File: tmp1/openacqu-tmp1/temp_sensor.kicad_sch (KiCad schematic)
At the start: 2 parts, among them J3 SJ-3524-SMT, U7 MCP9600T-E_MX

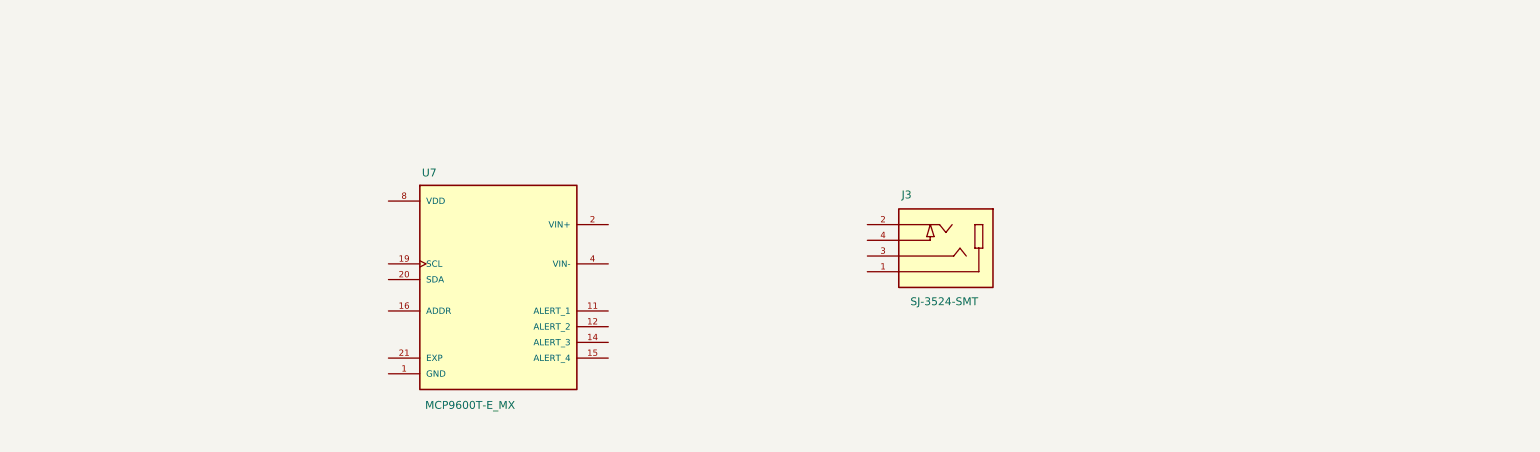
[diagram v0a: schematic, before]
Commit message: Completed layout for the TMP1
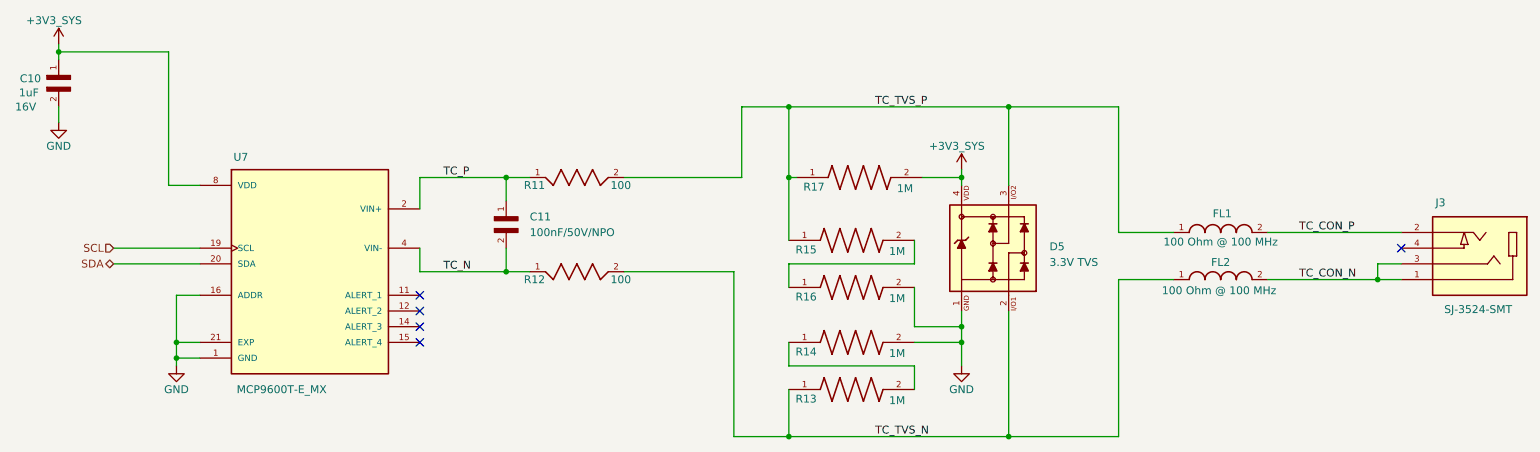
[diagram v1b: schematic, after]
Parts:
- added C10: 1uF, openacqu_footprints:CAPC1005X55N, symbol CL05A105KO5NNNC:CL05A105KO5NNNC
- added C11: 100nF/50V/NPO, CAPC3216X95N, symbol GRM3195C1H104JA05D:GRM3195C1H104JA05D
- added D5: 3.3V TVS, WE-TVS_SOT143-4L, symbol WE-TVS-HS_SOT143-4L_8240136:WE-TVS-HS_SOT143-4L_8240136
- added FL1, FL2: 100 Ohm @ 100 MHz, BEADC1608X65N, symbol BLM18EG101TN1D:BLM18EG101TN1D
- added R11, R12: 100, RESC1005X40, symbol RC0402FR-07100RL:RC0402FR-07100RL
- added R13, R14, R15, R16, R17: 1M, RESC1005X40N, symbol RC0402FR-071ML:RC0402FR-071ML
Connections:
- net GND is gone; now on net EXP: U7.1 (GND), U7.10 (GND), U7.13 (GND), U7.17 (GND), U7.18 (GND), U7.3 (GND), U7.5 (GND), U7.6 (GND), U7.7 (GND), U7.9 (GND)
- net EXP: now also U7.16 (ADDR), C10.2, D5.1, R14.2, R16.2
- net SCL: now reaches U7.19 (SCL)
- net TC_P: now reaches U7.2 (VIN+)
- net TC_P: now also C11.1, R11.1
- net SDA: now reaches U7.20 (SDA)
- net TC_N: now reaches U7.4 (VIN-)
- net TC_N: now also C11.2, R12.1
- net +3V3_SYS: now reaches U7.8 (VDD)
- net +3V3_SYS: now also C10.1, D5.4, R17.2
- net TC_CON_N: now reaches J3.1
- net TC_CON_N: now also J3.3, FL2.2
- net TC_CON_P: now reaches J3.2
- net TC_CON_P: now also FL1.2
- new net: R13.2, R14.1
- new net: R15.2, R16.1
- new net TC_TVS_N: D5.2, FL2.1, R12.2, R13.1
- new net TC_TVS_P: D5.3, FL1.1, R11.2, R15.1, R17.1
- no-connect marks 0 -> 5
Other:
- moved on the sheet: J3, U7

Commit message: Updated symbols with JLCPCB part numbers
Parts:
- C10: JLCPN (none) -> C29266
- C11: JLCPN (none) -> C363929
- D5: JLCPN (none) -> C1975797
- FL1, FL2: JLCPN (none) -> C76893
- J3: JLCPN (none) -> C20182907
- R11, R12: JLCPN (none) -> C106232
- R13, R14, R15, R16, R17: JLCPN (none) -> C138033
- U7: JLCPN (none) -> C623918
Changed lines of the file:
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@@
+			)
+		)
+		(property "JLCPN" "C623918"
+			(at 67.31 93.98 0)
+			(effects
+				(font
+					(size 1.27 1.27)
+				)
+				(hide yes)
 			)
 		)
@@
 			)
 		)
+		(property "JLCPN" "C20182907"
+			(at 256.54 88.9 0)
+			(effects
+				(font
+					(size 1.27 1.27)
+				)
+				(hide yes)
+			)
+		)
 		(pin "2"
 		)
@@
 			)
 		)
+		(property "JLCPN" "C76893"
+			(at 214.63 93.98 0)
+			(effects
+				(font
+					(size 1.27 1.27)
+				)
+				(hide yes)
+			)
+		)
 		(pin "1"
 		)
@@
 			)
 		)
+		(property "JLCPN" "C29266"
+			(at 26.67 60.96 0)
+			(effects
+				(font
+					(size 1.27 1.27)
+				)
+				(hide yes)
+			)
+		)
 		(pin "1"
 		)
@@
 			)
 		)
+		(property "JLCPN" "C138033"
+			(at 154.94 104.14 0)
+			(effects
+				(font
+					(size 1.27 1.27)
+				)
+				(hide yes)
+			)
+		)
 		(pin "1"
 		)
@@
 			)
 		)
+		(property "JLCPN" "C138033"
+			(at 154.94 87.63 0)
+			(effects
+				(font
+					(size 1.27 1.27)
+				)
+				(hide yes)
+			)
+		)
 		(pin "1"
 		)
@@
 			)
 		)
+		(property "JLCPN" "C1975797"
+			(at 177.8 88.9 0)
+			(effects
+				(font
+					(size 1.27 1.27)
+				)
+				(hide yes)
+			)
+		)
 		(pin "1"
 		)
@@
 				)
 				(justify bottom)
+				(hide yes)
+			)
+		)
+		(property "JLCPN" "C138033"
+			(at 154.94 111.76 0)
+			(effects
+				(font
+					(size 1.27 1.27)
+				)
 				(hide yes)
 			)
@@
 			)
 		)
+		(property "JLCPN" "C363929"
+			(at 99.06 83.82 0)
+			(effects
+				(font
+					(size 1.27 1.27)
+				)
+				(hide yes)
+			)
+		)
 		(pin "1"
 		)
@@
 			)
 		)
+		(property "JLCPN" "C138033"
+			(at 154.94 95.25 0)
+			(effects
+				(font
+					(size 1.27 1.27)
+				)
+				(hide yes)
+			)
+		)
 		(pin "1"
 		)
@@
 			)
 		)
+		(property "JLCPN" "C106232"
+			(at 110.49 92.71 0)
+			(effects
+				(font
+					(size 1.27 1.27)
+				)
+				(hide yes)
+			)
+		)
 		(pin "1"
 		)
@@
 			)
 		)
+		(property "JLCPN" "C76893"
+			(at 214.63 86.36 0)
+			(effects
+				(font
+					(size 1.27 1.27)
+				)
+				(hide yes)
+			)
+		)
 		(pin "1"
 		)
@@
 			)
 		)
+		(property "JLCPN" "C138033"
+			(at 156.21 77.47 0)
+			(effects
+				(font
+					(size 1.27 1.27)
+				)
+				(hide yes)
+			)
+		)
 		(pin "1"
 		)
@@
 				(hide yes)
 			)
+		)
+		(property "JLCPN" "C106232"
+			(at 110.49 77.47 0)
+			(effects
+				(font
+					(size 1.27 1.27)
+				)
+				(hide yes)
+			)
